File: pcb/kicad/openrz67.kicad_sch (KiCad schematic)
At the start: 59 parts, among them U1 ESP32-C3FH4, U3 LGS5500EP, U4 S4B-XH-A(LF)(SN), U5 TLP172GM, U6 TLP172GM, X1 40MHz, X2 32.768kHz

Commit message: Update rev 2 PCB layout
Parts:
- BAT1: value S2B-PH-SM4-TB(LF)(SN) -> B2B-PH-K-S(LF)(SN); footprint openrz67:CONN-SMD_P2.00_S2B-PH-SM4-TB-LF-SN -> openrz67:CONN-TH_B2B-PH-K-S; symbol openrz67:S2B-PH-SM4-TB -> openrz67:B2B-PH-K-S(LF)(SN); LCSC Part Name 2P PH SMD side-entry 2.0mm -> 1x2P 间距:2mm 直插 系列:PH; Manufacturer Part S2B-PH-SM4-TB(LF)(SN) -> B2B-PH-K-S(LF)(SN); Supplier Part C295747 -> C131337

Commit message: Revert "Update rev 2 PCB layout"
This reverts commit d763081e84975234f8d2c617ac684d1041c5a9e0.
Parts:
- BAT1: value B2B-PH-K-S(LF)(SN) -> S2B-PH-SM4-TB(LF)(SN); footprint openrz67:CONN-TH_B2B-PH-K-S -> openrz67:CONN-SMD_P2.00_S2B-PH-SM4-TB-LF-SN; symbol openrz67:B2B-PH-K-S(LF)(SN) -> openrz67:S2B-PH-SM4-TB; LCSC Part Name 1x2P 间距:2mm 直插 系列:PH -> 2P PH SMD side-entry 2.0mm; Manufacturer Part B2B-PH-K-S(LF)(SN) -> S2B-PH-SM4-TB(LF)(SN); Supplier Part C131337 -> C295747

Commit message: Use lower-resistance PhotoMOS relays
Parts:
- U5, U6: value TLP172GM -> TLP172AM; symbol openrz67:TLP172GM -> openrz67:TLP172AM; LCSC Part Name TLP172GM(TPL,E -> TLP172AM(TPL,E; Manufacturer Part TLP172GM(TPL,E -> TLP172AM(TPL,E; Supplier Part C261926 -> C2152276

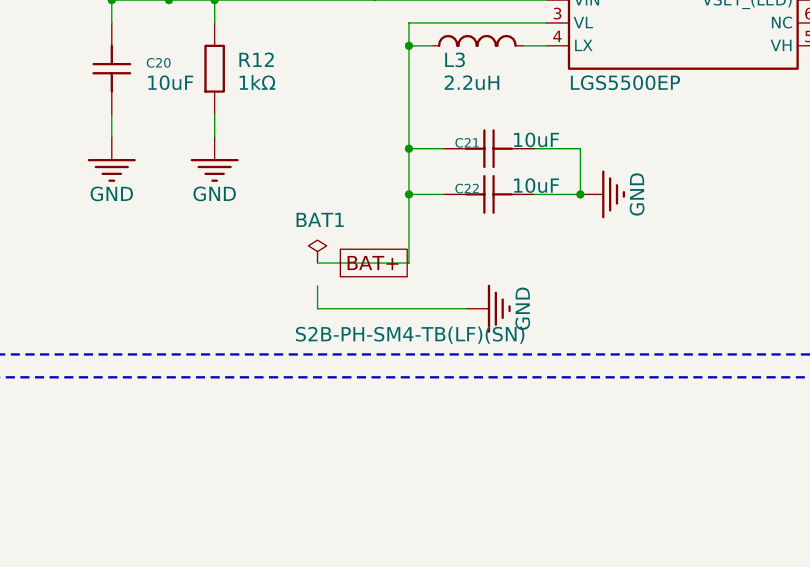
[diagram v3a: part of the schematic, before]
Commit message: Move battery connector back to top
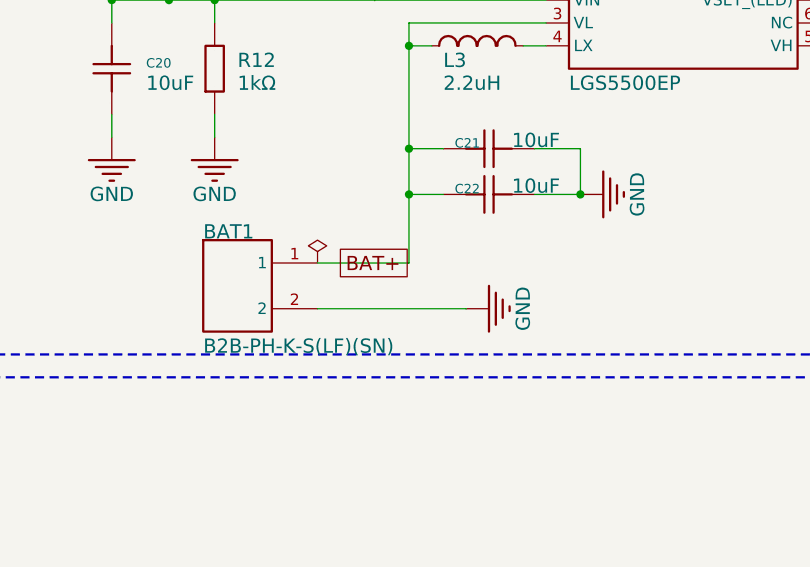
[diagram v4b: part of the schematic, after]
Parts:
- BAT1: value S2B-PH-SM4-TB(LF)(SN) -> B2B-PH-K-S(LF)(SN); footprint openrz67:CONN-SMD_P2.00_S2B-PH-SM4-TB-LF-SN -> openrz67:CONN-TH_B2B-PH-K-S; symbol openrz67:S2B-PH-SM4-TB -> openrz67:B2B-PH-K-S(LF)(SN); LCSC Part Name 2P PH SMD side-entry 2.0mm -> 1x2P 间距:2mm 直插 系列:PH; Manufacturer Part S2B-PH-SM4-TB(LF)(SN) -> B2B-PH-K-S(LF)(SN); Supplier Part C295747 -> C131337
